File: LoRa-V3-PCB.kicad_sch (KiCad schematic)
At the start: 88 parts, among them IC1 SeeedStudio Wio-E5-LE-HF, IC10 BR24G1MFVT-5AE2, IC11 BR24G1MFVT-5AE2, IC12 MCP73123T-22SI/MF, IC2 CP2102N-Axx-xQFN24, IC3 USBLC6-2P6, IC4 BQ25504RGTR, IC5 BME680, IC6 SHT40-BD1B-R2, IC7 TSL25911FN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

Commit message: update on USB ESD protection - partnumber
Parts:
- IC3: manufacturerPartNumber USBLC6-2P6 -> USBLC6-2SC6; octopartUrl https://octopart.com/usblc6-2p6-stmicroelectronics-347175?r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 -> https://octopart.com/usblc6-2sc6-stmicroelectronics-39666276
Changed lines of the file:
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@@
 			)
 		)
-		(property "Datasheet" "https://datasheet.lcsc.com/szlcsc/STMicroelectronics-USBLC6-2P6_C15999.pdf"
+		(property "Datasheet" "https://www.mouser.be/datasheet/2/389/usblc6_2-1852789.pdf"
 			(at 76.2 414.63 0)
 			(effects
@@
 			)
 		)
-		(property "octopartUrl" "https://octopart.com/usblc6-2p6-stmicroelectronics-347175?r=sp"
+		(property "octopartUrl" "https://octopart.com/usblc6-2sc6-stmicroelectronics-39666276"
 			(at 105.41 219.71 0)
 			(effects
@@
 			)
 		)
-		(property "manufacturerPartNumber" "USBLC6-2P6"
+		(property "manufacturerPartNumber" "USBLC6-2SC6"
 			(at 105.41 219.71 0)
 			(effects

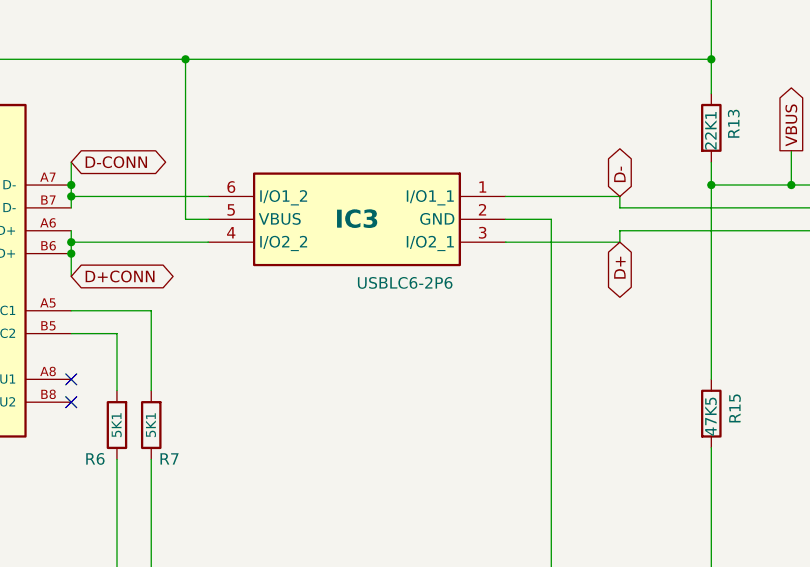
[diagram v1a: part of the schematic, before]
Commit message: cleanup bom on IC3
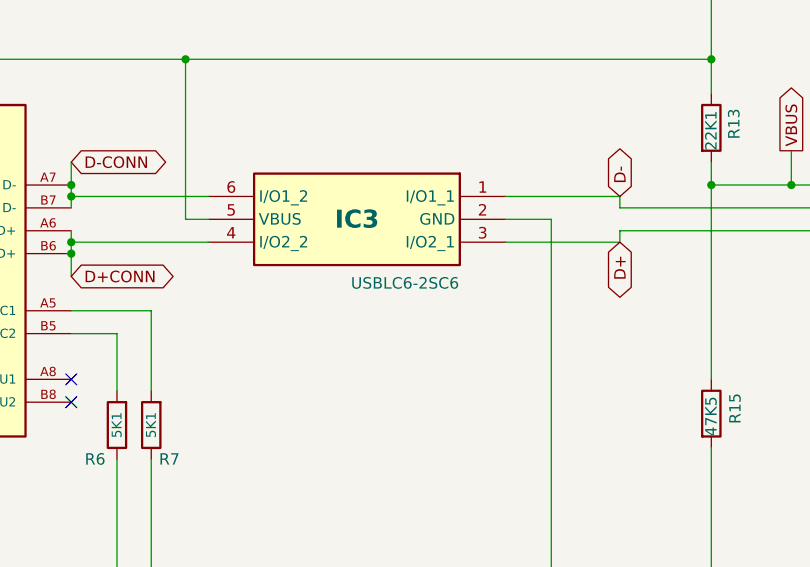
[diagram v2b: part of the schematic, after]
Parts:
- IC3: value USBLC6-2P6 -> USBLC6-2SC6; symbol 1projectLibrary:USBLC6-2P6 -> 1projectLibrary:USBLC6-2SC6
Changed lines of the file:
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@@
 	)
 	(symbol
-		(lib_id "1projectLibrary:USBLC6-2P6")
+		(lib_id "1projectLibrary:USBLC6-2SC6")
 		(at 105.41 219.71 0)
 		(mirror y)
@@
 			)
 		)
-		(property "Value" "USBLC6-2P6"
+		(property "Value" "USBLC6-2SC6"
 			(at 110.744 226.822 0)
 			(effects

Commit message: routing complete
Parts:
- removed C3, C4: 100nF, 1projectLibrary:C_0603_nominal, symbol Device:C
- removed IC5: BME680, 1projectLibrary:BME680, symbol 1projectLibrary:BME680
- removed IC6: SHT40-BD1B-R2, 1projectLibrary:SHT4X, symbol 1projectLibrary:SHT40
- removed IC7: TSL25911FN, 1projectLibrary:TSL2591, symbol 1projectLibrary:TSL2591
- added CONN7: Sensors, 1projectLibrary:GCT_BC075-08-A-L-A, symbol 1projectLibrary:Conn_01x08_Sensors
- CONN8: footprint 1projectLibrary:DebugPort-6P-2.54 -> 1projectLibrary:Debug_PinHeader_1x06_P2.00mm_Vertical
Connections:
- net +3.3V: now also CONN8.2 (Pin_2); no longer CONN8.1 (Pin_1)
- net GND: now also CONN8.1 (Pin_1), CONN7.1 (Pin_1), CONN7.8 (Pin_8); no longer CONN8.2 (Pin_2)
- net I2C2-SCL: now also CONN7.3 (Pin_3), CONN7.6 (Pin_6)
- net I2C2-SDA: now also CONN7.4 (Pin_4), CONN7.5 (Pin_5)
- net SWCLK: now also CONN8.3 (Pin_3); no longer CONN8.4 (Pin_4)
- net SWDIO: now also CONN8.4 (Pin_4); no longer CONN8.3 (Pin_3)
- net SWO: now also CONN8.6 (Pin_6); no longer CONN8.5 (Pin_5)
- net UART1-TX: now also CONN8.5 (Pin_5); no longer CONN8.6 (Pin_6)
- net VDD-SENSORS-EEPROM: now also CONN7.2 (Pin_2), CONN7.7 (Pin_7)
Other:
- note removed: "PCB Sensors"

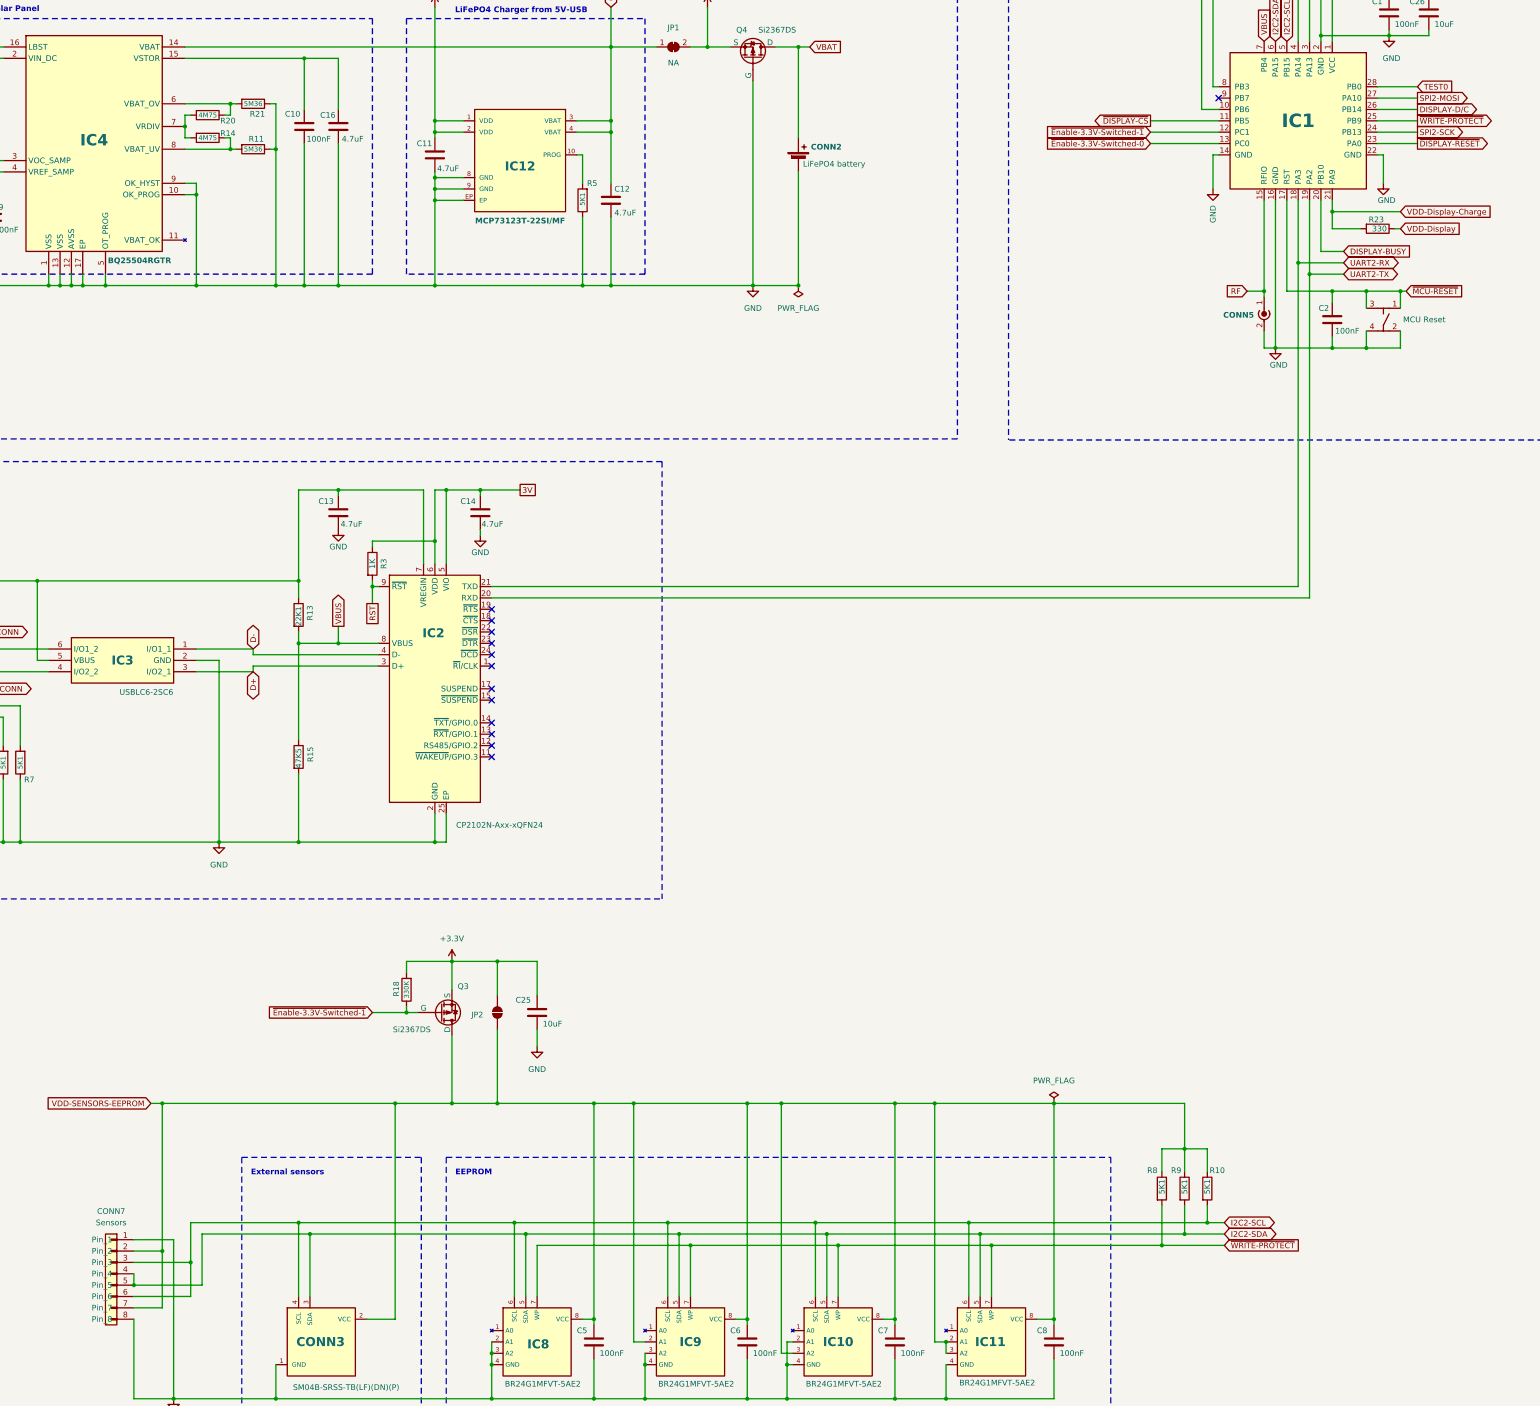
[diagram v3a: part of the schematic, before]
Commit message: correct pins on sensor connector
SDA and SCL were reversed
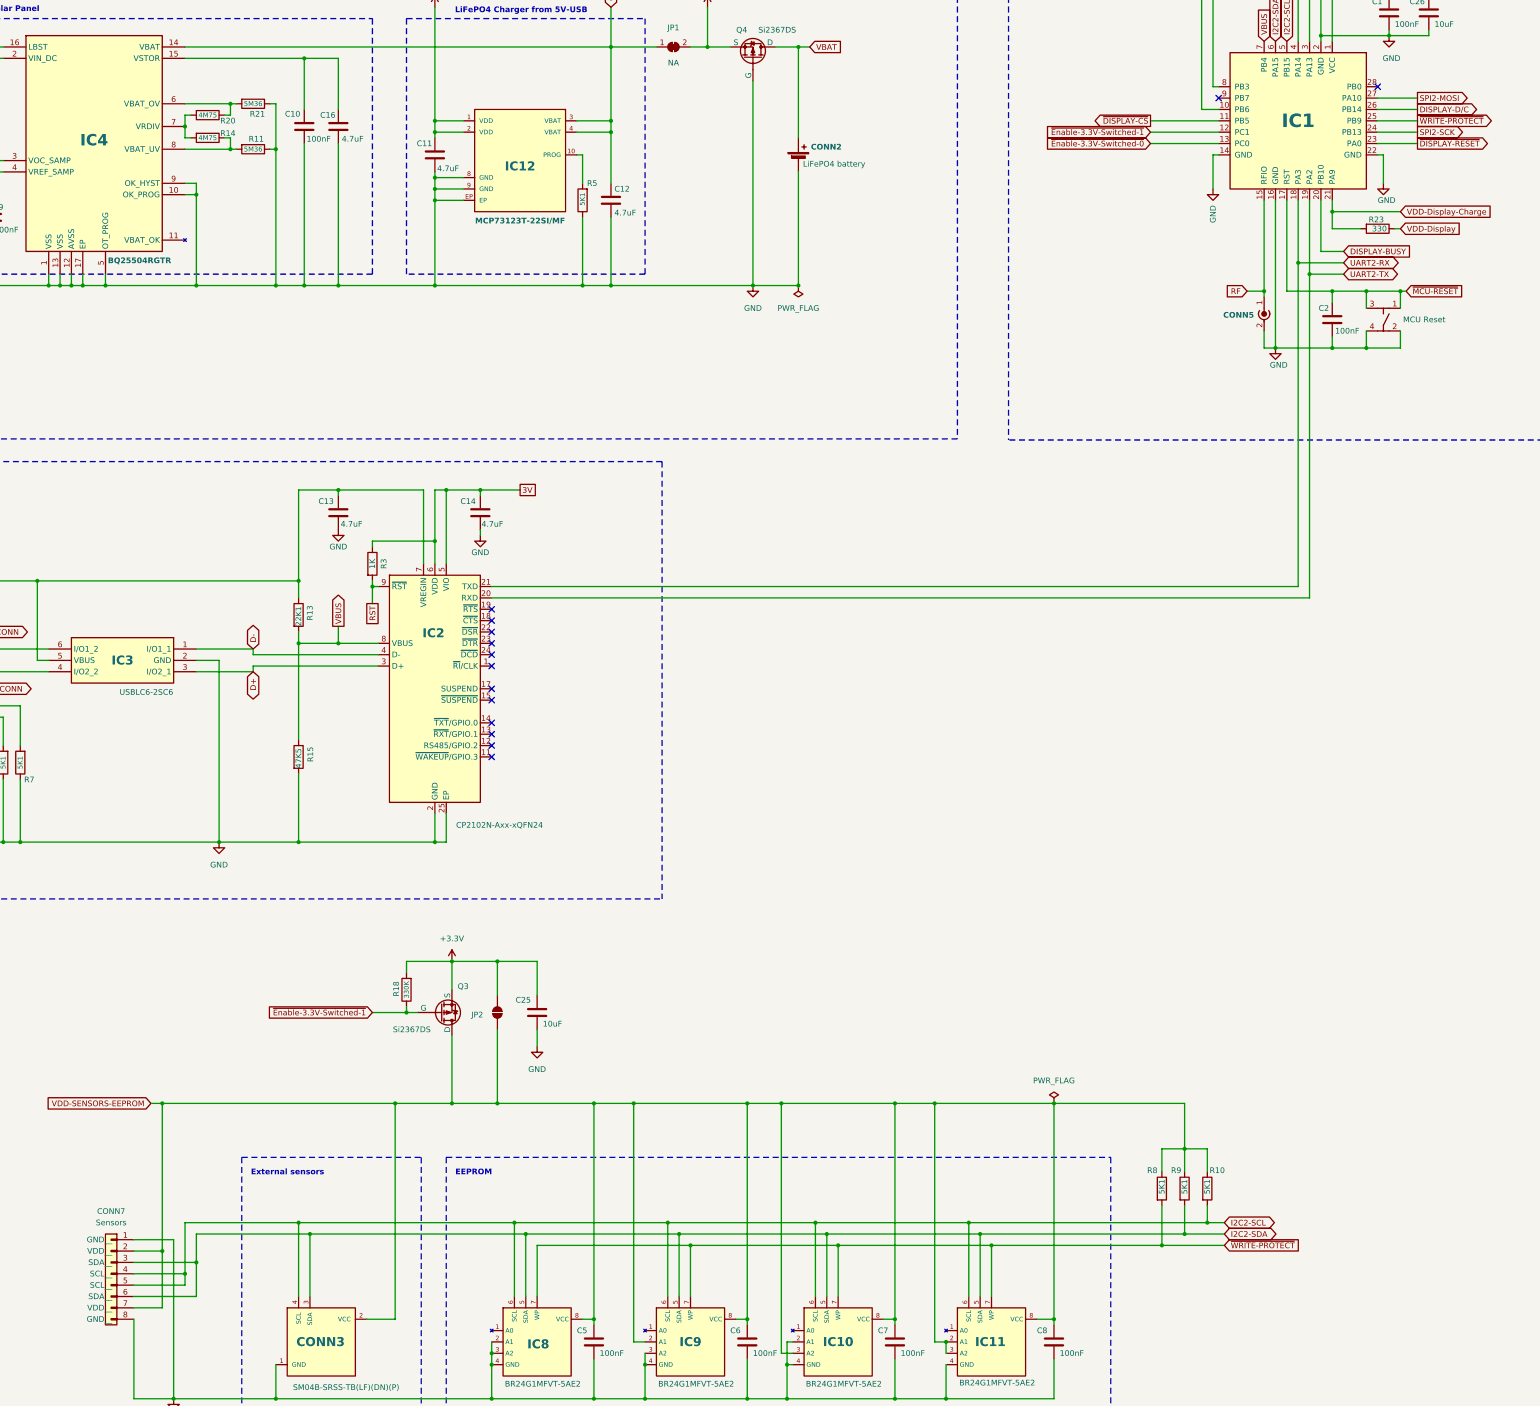
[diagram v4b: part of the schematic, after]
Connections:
- net I2C2-SCL: now also CONN7.4 (SCL__), CONN7.5 (SCL__); no longer CONN7.3 (Pin_3), CONN7.6 (Pin_6)
- net I2C2-SDA: now also CONN7.3 (SDA__), CONN7.6 (SDA__); no longer CONN7.4 (Pin_4), CONN7.5 (Pin_5)
- net TEST0: no longer names the net of IC1.28 (PB0)
- no-connect marks 23 -> 24
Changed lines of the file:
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@@
 	)
 	(junction
-		(at 120.65 354.33)
-		(diameter 0)
-		(color 0 0 0 0)
-	)
-	(junction
 		(at 532.13 86.36)
 		(diameter 0)
@@
 	)
 	(junction
+		(at 121.92 354.33)
+		(diameter 0)
+		(color 0 0 0 0)
+	)
+	(junction
 		(at 168.91 298.45)
 		(diameter 0)
@@
 	)
 	(junction
-		(at 107.95 359.41)
-		(diameter 0)
-		(color 0 0 0 0)
-	)
-	(junction
 		(at 375.92 149.86)
 		(diameter 0)
@@
 	)
 	(junction
+		(at 119.38 356.87)
+		(diameter 0)
+		(color 0 0 0 0)
+	)
+	(junction
 		(at 179.07 318.77)
 		(diameter 0)
@@
 	)
 	(no_connect
+		(at 386.08 91.44)
+	)
+	(no_connect
 		(at 46.99 251.46)
 	)
@@
 	(wire
 		(pts
-			(xy 107.95 361.95) (xy 120.65 361.95)
+			(xy 107.95 361.95) (xy 121.92 361.95)
 		)
 		(stroke
@@
 	(wire
 		(pts
-			(xy 120.65 354.33) (xy 107.95 354.33)
-		)
-		(stroke
-			(width 0)
-			(type default)
-		)
-	)
-	(wire
-		(pts
 			(xy 121.92 115.57) (xy 121.92 135.89)
 		)
@@
 	(wire
 		(pts
+			(xy 119.38 359.41) (xy 119.38 356.87)
+		)
+		(stroke
+			(width 0)
+			(type default)
+		)
+	)
+	(wire
+		(pts
 			(xy 289.56 372.11) (xy 287.02 372.11)
 		)
@@
 	(wire
 		(pts
-			(xy 123.19 347.98) (xy 147.32 347.98)
+			(xy 121.92 347.98) (xy 147.32 347.98)
 		)
 		(stroke
@@
 	(wire
 		(pts
+			(xy 119.38 345.44) (xy 144.78 345.44)
+		)
+		(stroke
+			(width 0)
+			(type default)
+		)
+	)
+	(wire
+		(pts
 			(xy 62.23 260.35) (xy 78.74 260.35)
 		)
@@
 	(wire
 		(pts
-			(xy 123.19 359.41) (xy 107.95 359.41)
-		)
-		(stroke
-			(width 0)
-			(type default)
-		)
-	)
-	(wire
-		(pts
 			(xy 513.08 100.33) (xy 513.08 91.44)
 		)
@@
 	(wire
 		(pts
+			(xy 107.95 356.87) (xy 119.38 356.87)
+		)
+		(stroke
+			(width 0)
+			(type default)
+		)
+	)
+	(wire
+		(pts
 			(xy 232.41 350.52) (xy 265.43 350.52)
 		)
@@
 	(wire
 		(pts
+			(xy 107.95 359.41) (xy 119.38 359.41)
+		)
+		(stroke
+			(width 0)
+			(type default)
+		)
+	)
+	(wire
+		(pts
 			(xy 502.92 151.13) (xy 508 151.13)
 		)
@@
 	(wire
 		(pts
-			(xy 123.19 347.98) (xy 123.19 359.41)
-		)
-		(stroke
-			(width 0)
-			(type default)
-		)
-	)
-	(wire
-		(pts
 			(xy 508 91.44) (xy 508 100.33)
 		)
@@
 	(wire
 		(pts
-			(xy 175.26 111.76) (xy 181.61 111.76)
+			(xy 121.92 354.33) (xy 107.95 354.33)
 		)
 		(stroke
@@
 	(wire
 		(pts
-			(xy 373.38 80.01) (xy 373.38 81.28)
+			(xy 175.26 111.76) (xy 181.61 111.76)
 		)
 		(stroke
@@
 	(wire
 		(pts
-			(xy 120.65 345.44) (xy 120.65 354.33)
+			(xy 373.38 80.01) (xy 373.38 81.28)
 		)
 		(stroke
@@
 	(wire
 		(pts
-			(xy 107.95 356.87) (xy 107.95 359.41)
-		)
-		(stroke
-			(width 0)
-			(type default)
-		)
-	)
-	(wire
-		(pts
 			(xy 524.51 91.44) (xy 524.51 93.98)
 		)
@@
 	(wire
 		(pts
-			(xy 120.65 345.44) (xy 144.78 345.44)
+			(xy 539.75 134.62) (xy 539.75 157.48)
 		)
 		(stroke
@@
 	(wire
 		(pts
-			(xy 539.75 134.62) (xy 539.75 157.48)
+			(xy 502.92 142.24) (xy 502.92 134.62)
 		)
 		(stroke
@@
 	(wire
 		(pts
-			(xy 502.92 142.24) (xy 502.92 134.62)
+			(xy 121.92 219.71) (xy 127 219.71)
 		)
 		(stroke
@@
 	(wire
 		(pts
-			(xy 121.92 219.71) (xy 127 219.71)
+			(xy 487.68 91.44) (xy 487.68 100.33)
 		)
 		(stroke
@@
 	(wire
 		(pts
-			(xy 487.68 91.44) (xy 487.68 100.33)
+			(xy 544.83 139.7) (xy 547.37 139.7)
 		)
 		(stroke
@@
 	(wire
 		(pts
-			(xy 544.83 139.7) (xy 547.37 139.7)
+			(xy 82.55 260.35) (xy 127 260.35)
 		)
 		(stroke
@@
 	(wire
 		(pts
-			(xy 82.55 260.35) (xy 127 260.35)
+			(xy 121.92 354.33) (xy 121.92 347.98)
 		)
 		(stroke
@@
 	(wire
 		(pts
-			(xy 386.08 91.44) (xy 394.97 91.44)
-		)
-		(stroke
-			(width 0)
-			(type default)
-		)
-	)
-	(wire
-		(pts
 			(xy 375.92 69.85) (xy 388.62 69.85)
 		)
@@
 	(wire
 		(pts
-			(xy 120.65 361.95) (xy 120.65 354.33)
+			(xy 121.92 361.95) (xy 121.92 354.33)
 		)
 		(stroke
@@
 	(wire
 		(pts
+			(xy 119.38 356.87) (xy 119.38 345.44)
+		)
+		(stroke
+			(width 0)
+			(type default)
+		)
+	)
+	(wire
+		(pts
 			(xy 481.33 151.13) (xy 487.68 151.13)
 		)
@@
 				(hide yes)
 			)
-		)
-	)
-	(global_label "TEST0"
-		(shape input)
-		(at 394.97 91.44 0)
-		(fields_autoplaced yes)
-		(effects
-			(font
-				(size 1.27 1.27)
-			)
-			(justify left)
-		)
-		(property "Intersheetrefs" "${INTERSHEET_REFS}"
-			(at 403.4584 91.44 0)
-			(effects
-				(font
-					(size 1.27 1.27)
-				)
-				(justify left)
-				(hide yes)
-			)

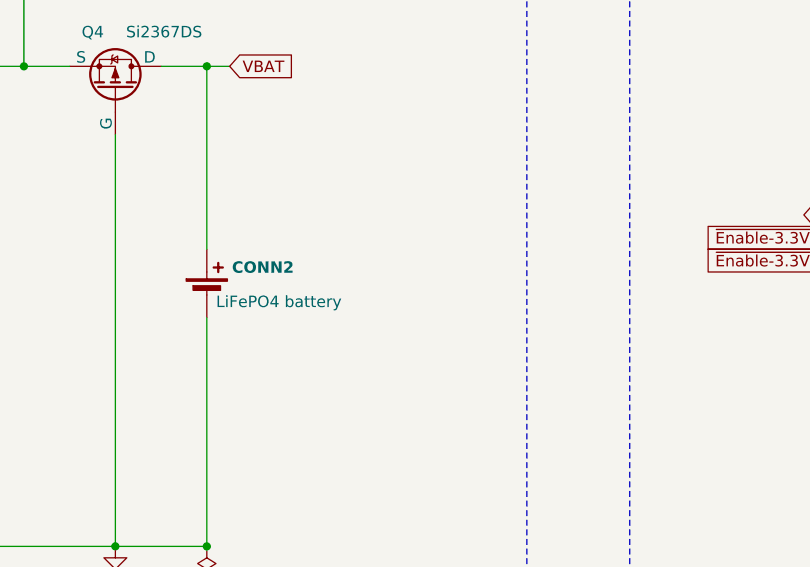
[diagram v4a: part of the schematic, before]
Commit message: replace battery holder
to Keystone 2460
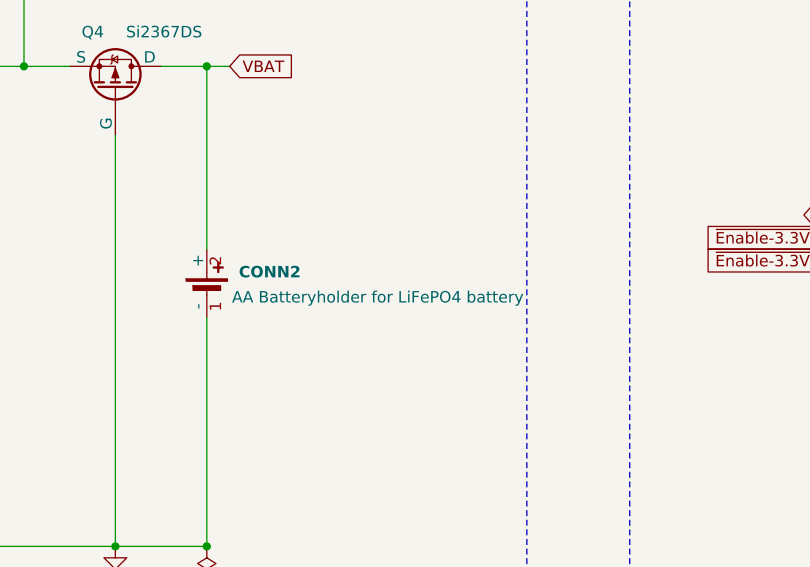
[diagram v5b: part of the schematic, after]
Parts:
- CONN2: value LiFePO4 battery -> AA Batteryholder for LiFePO4 battery; footprint 1projectLibrary:Keystone 1015 AA BatteryHolder -> 1projectLibrary:BAT_2460; manufacturerPartNumber 1015 -> 2460; octopartUrl https://octopart.com/1015-keystone-8129901?r=sp -> https://octopart.com/2460-keystone-17876
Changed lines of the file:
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@@
 		(dnp no)
 		(property "Reference" "CONN2"
-			(at 259.334 104.902 0)
+			(at 260.096 105.41 0)
 			(effects
 				(font
@@
 			)
 		)
-		(property "Value" "LiFePO4 battery"
-			(at 257.556 108.712 0)
+		(property "Value" "AA Batteryholder for LiFePO4 battery"
+			(at 259.334 108.204 0)
 			(effects
 				(font
@@
 			)
 		)
-		(property "Footprint" "1projectLibrary:Keystone 1015 AA BatteryHolder"
+		(property "Footprint" "1projectLibrary:BAT_2460"
 			(at 248.92 105.41 90)
 			(effects
@@
 			)
 		)
-		(property "Datasheet" "https://www.keyelco.com/userAssets/file/M65p22.pdf"
+		(property "Datasheet" "https://www.mouser.be/datasheet/2/215/2460-741228.pdf"
 			(at 269.24 107.95 90)
 			(effects
@@
 			)
 		)
-		(property "octopartUrl" "https://octopart.com/1015-keystone-8129901?r=sp"
+		(property "octopartUrl" "https://octopart.com/2460-keystone-17876"
 			(at 264.16 113.03 0)
 			(effects
@@
 			)
 		)
-		(property "manufacturerPartNumber" "1015"
+		(property "manufacturerPartNumber" "2460"
 			(at 264.16 118.11 0)
 			(effects
